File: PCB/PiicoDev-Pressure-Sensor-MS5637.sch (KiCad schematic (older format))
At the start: 19 parts, among them J1 , J2 , J3 Conn_PiicoDev_header_01x04_Ma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, U1 MS5637

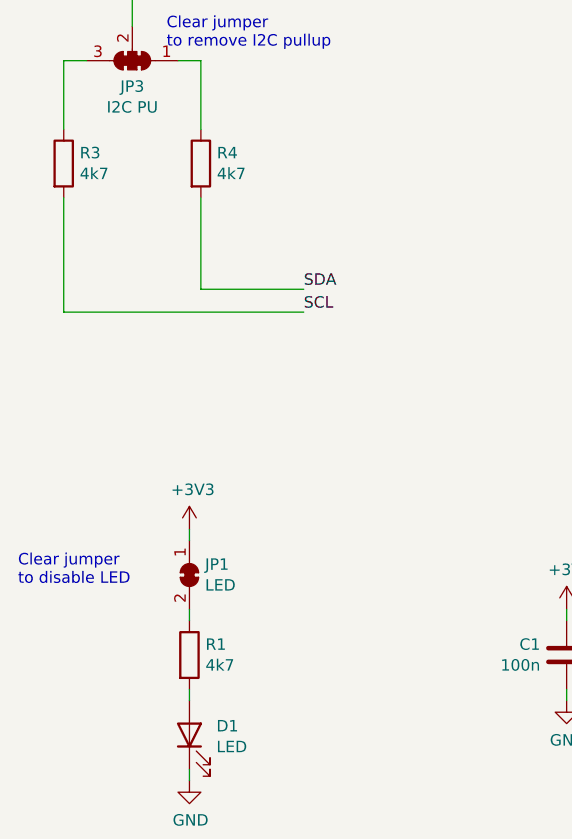
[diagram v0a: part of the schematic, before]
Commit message: Change 4k7 resistors to 10k
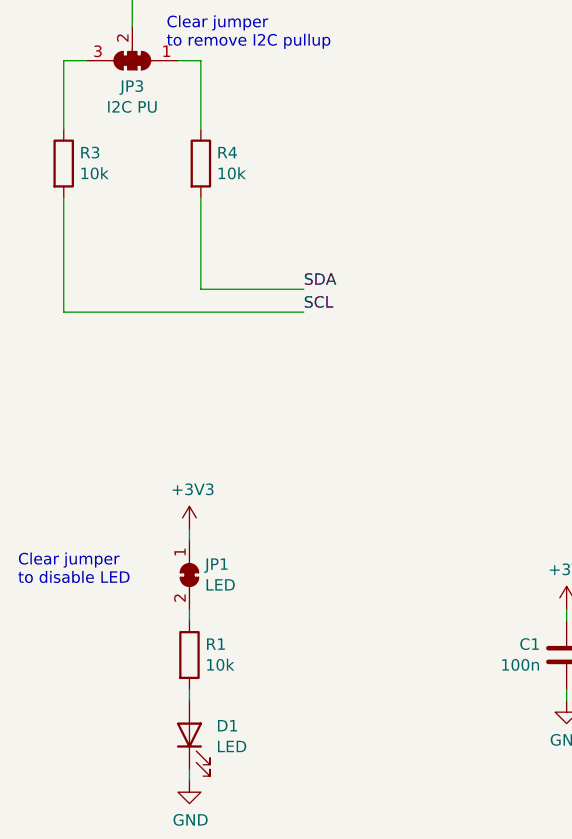
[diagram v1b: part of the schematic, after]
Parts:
- R1, R3, R4: value 4k7 -> 10k
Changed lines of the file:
@@
 P 2250 1600
 F 0 "R4" H 2320 1646 50  0000 L CNN
-F 1 "4k7" H 2320 1555 50  0000 L CNN
+F 1 "10k" H 2320 1555 50  0000 L CNN
 F 2 "Resistor_SMD:R_0402_1005Metric" V 2180 1600 50  0001 C CNN
 F 3 "~" H 2250 1600 50  0001 C CNN
@@
 P 1650 1600
 F 0 "R3" H 1720 1646 50  0000 L CNN
-F 1 "4k7" H 1720 1555 50  0000 L CNN
+F 1 "10k" H 1720 1555 50  0000 L CNN
 F 2 "Resistor_SMD:R_0402_1005Metric" V 1580 1600 50  0001 C CNN
 F 3 "~" H 1650 1600 50  0001 C CNN
@@
 P 2200 3750
 F 0 "R1" H 2270 3796 50  0000 L CNN
-F 1 "4k7" H 2270 3705 50  0000 L CNN
+F 1 "10k" H 2270 3705 50  0000 L CNN
 F 2 "Resistor_SMD:R_0402_1005Metric" V 2130 3750 50  0001 C CNN
 F 3 "~" H 2200 3750 50  0001 C CNN
